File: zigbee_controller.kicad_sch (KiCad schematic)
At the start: 57 parts, among them J1 +24V, J10 IO23 load, J12 IO2 load, J13 IO, J2 5v, J4 Conn_01x07, J5 Conn_01x05, J9 IO0 load, P1 USB_C_Plug_USB2.0, Q1 IRLZ44n, Q2 IRLZ44n, Q3 IRLZ44n, SW2 EN, SW4 Joint download Boot mode, U1 TPS54560, U2 ESP32-C6-MINI-1, U3 AMS1117-3.3

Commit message: Crashed
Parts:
- removed C11, C12, C8: 22μF, Capacitor_SMD:C_1206_3216Metric_Pad1.33x1.80mm_HandSolder, symbol Device:C
- removed J13: IO, Connector_JST:JST_XH_B4B-XH-A_1x04_P2.50mm_Vertical, symbol Connector_Generic:Conn_01x04
- added C16, C17: 2.2uF, Capacitor_SMD:C_1206_3216Metric_Pad1.33x1.80mm_HandSolder, symbol Device:C
- added J3: Conn_01x06, Connector_JST:JST_XH_B6B-XH-A_1x06_P2.50mm_Vertical, symbol Connector_Generic:Conn_01x06
- added Q4, Q5, Q6: MMBT3904, Package_TO_SOT_SMD:SOT-23, symbol Transistor_BJT:MMBT3904
- added Q7: MMBT3906, Package_TO_SOT_SMD:SOT-23, symbol Transistor_BJT:MMBT3906
- added R16: 3K, symbol Device:R
- added R17: 33K, symbol Device:R
- C1, C2: value 4.7uF -> 2.2uF
- C10, C4, C9: value 22μF -> 4.7μF
- C3: value (none) -> 2.2uF; now fitted; now in the parts list
- J1, J10, J12: footprint Connector_JST:JST_VH_B2PS-VH_1x02_P3.96mm_Horizontal -> TerminalBlock:MKDS 1,5 2-5,08 P2
- J9: value IO0 load -> IO1 load; footprint Connector_JST:JST_VH_B2PS-VH_1x02_P3.96mm_Horizontal -> TerminalBlock:MKDS 1,5 2-5,08 P2
- L1: value 2.2μH -> 22μH; footprint Inductor_SMD:L_Changjiang_FXL0650 -> Inductor_SMD:L_Bourns-SRN8040_8x8.15mm
- P1: footprint Connector_USB:USB_C_Plug_ShenzhenJingTuoJin_918-118A2021Y40002_Vertical -> Connector_USB:USB_C_Receptacle_GCT_USB4105-xx-A_16P_TopMnt_Horizontal
- Q1, Q2, Q3: value IRLZ44n -> IRLB8721; footprint Package_TO_SOT_SMD:TO-263-3_TabPin2 -> Package_TO_SOT_THT:TO-220-3_Vertical
- R2: value 100k -> 51k
- R3: value 68K -> 200k
- R7: value 470k -> 220k
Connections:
- net +24V: now also C16.1, C17.1; no longer J9.1 (Pin_1)
- net +5V: now also Q4.3 (C)
- net 3V3: now also J3.1 (Pin_1)
- net GND: now also J4.7 (Pin_7), C16.2, C17.2, J3.6 (Pin_6), Q7.3 (C), R17.2; no longer J4.1 (Pin_1)
- net IO0: now also J3.4 (Pin_4); no longer J5.4 (Pin_4)
- net IO1: now also J3.5 (Pin_5), R16.1, R17.1; no longer J5.3 (Pin_3), R9.2
- net IO12-usb: now also J4.4 (Pin_4); no longer J5.2 (Pin_2)
- net IO13-usb: now also J4.3 (Pin_3); no longer J5.1 (Pin_1)
- net IO2: now also J3.2 (Pin_2)
- net IO20: now also J5.1 (Pin_1); no longer J4.7 (Pin_7)
- net IO21: now also J5.2 (Pin_2); no longer J4.6 (Pin_6)
- net IO22: now also J4.6 (Pin_6); no longer J4.5 (Pin_5)
- net IO23: now also J4.5 (Pin_5); no longer J4.4 (Pin_4)
- net IO3: now also J3.3 (Pin_3)
- net RX: now also J4.2 (Pin_2); no longer J4.3 (Pin_3)
- net TX: now also J4.1 (Pin_1); no longer J4.2 (Pin_2)
- new net: Q4.2 (E), Q7.2 (E), R9.2
- new net: Q4.1 (B), Q7.1 (B), R16.2
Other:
- moved on the sheet: J1, J9, Q1, R5, R9

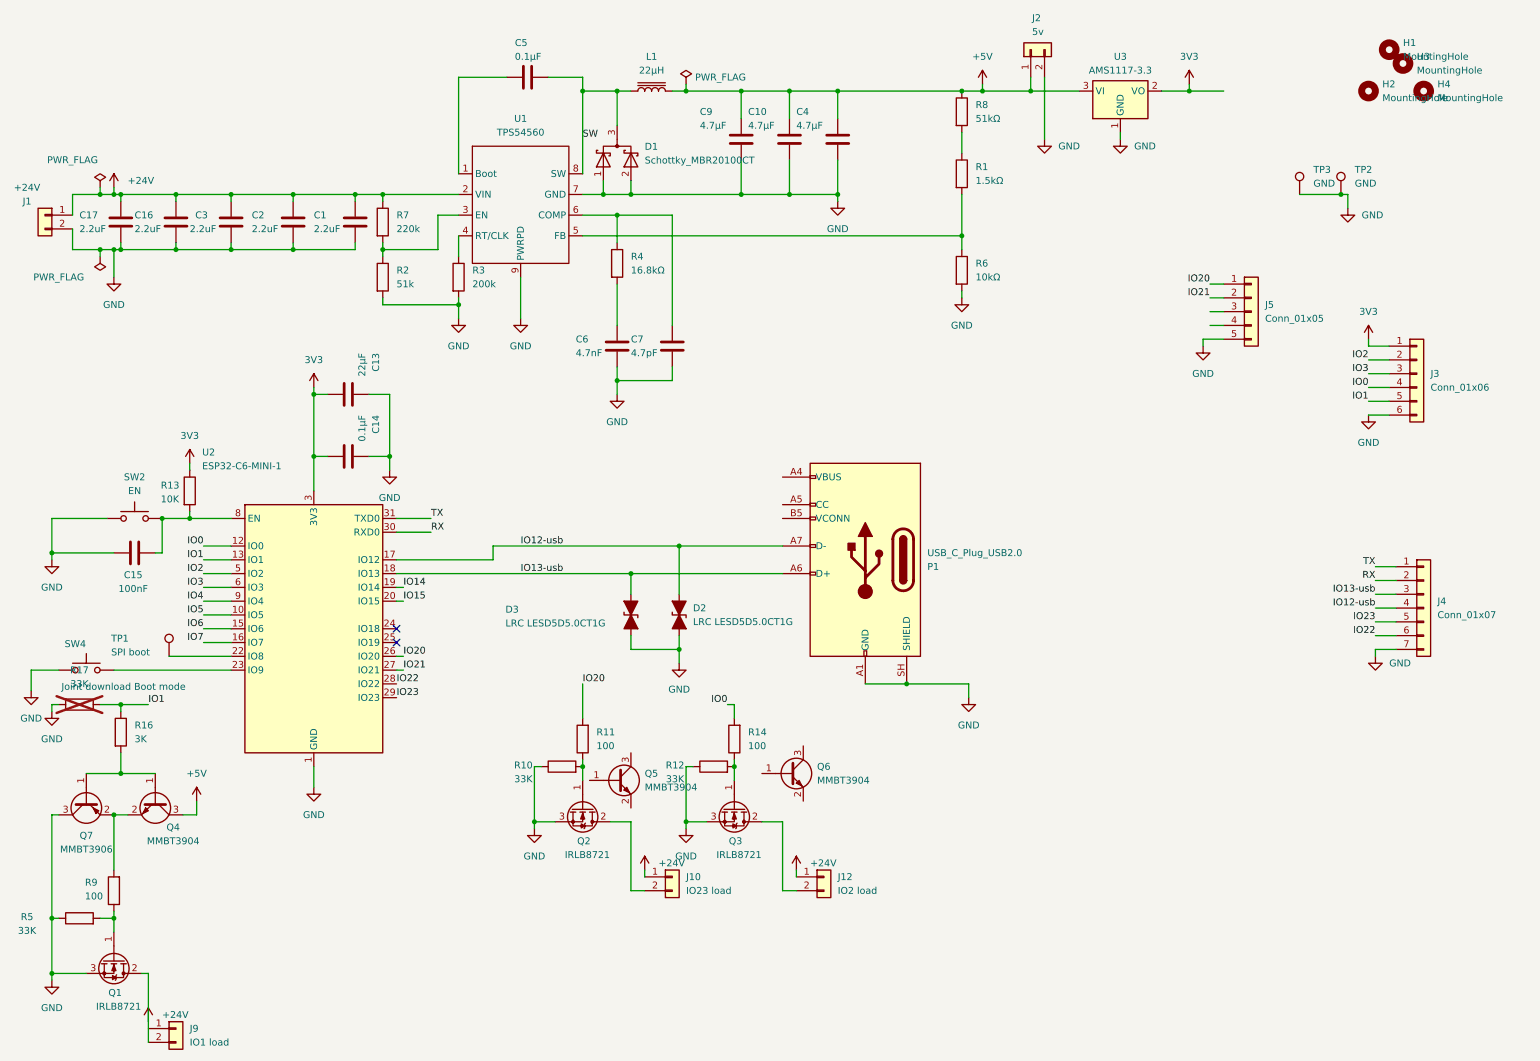
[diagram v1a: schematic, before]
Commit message: All working,  but copper pure current bottleneck
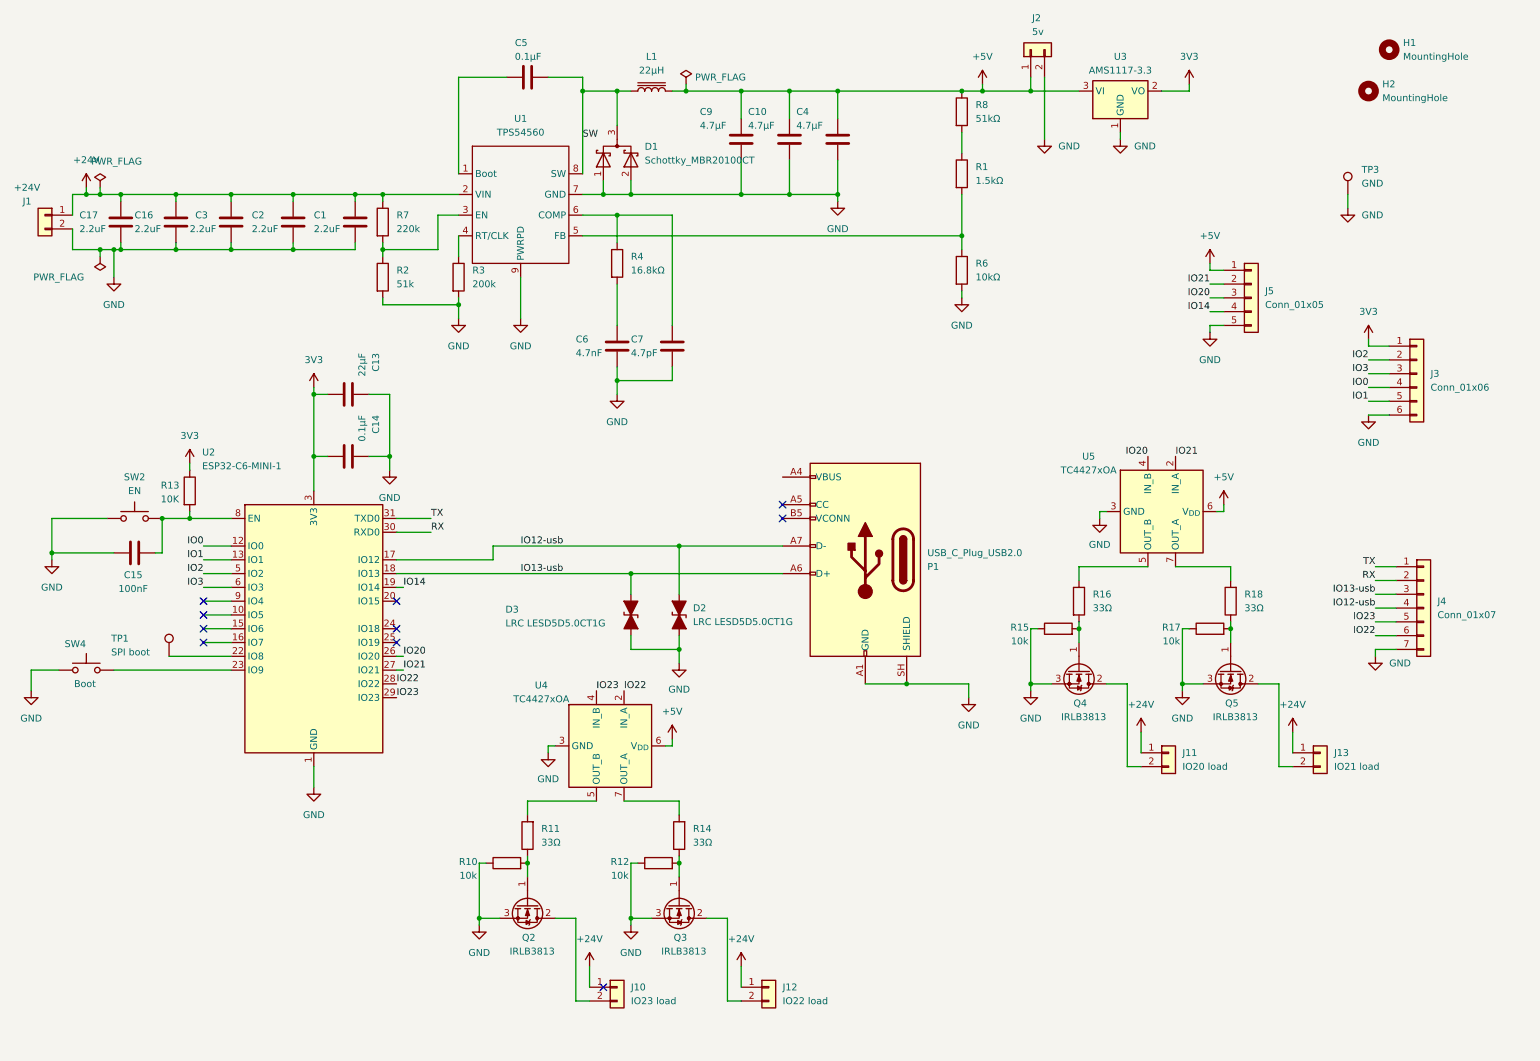
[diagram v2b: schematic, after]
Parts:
- removed H3, H4: MountingHole, MountingHole:MountingHole_2mm, symbol Mechanical:MountingHole
- removed J9: IO1 load, TerminalBlock:MKDS 1,5 2-5,08 P2, symbol Connector_Generic:Conn_01x02
- removed Q1: IRLB8721, Package_TO_SOT_THT:TO-220-3_Vertical, symbol davouds_symbol_library:IRLZ44NS
- removed Q4, Q5, Q6: MMBT3904, Package_TO_SOT_SMD:SOT-23, symbol Transistor_BJT:MMBT3904
- removed Q7: MMBT3906, Package_TO_SOT_SMD:SOT-23, symbol Transistor_BJT:MMBT3906
- removed R5: 33K, Resistor_SMD:R_1206_3216Metric_Pad1.30x1.75mm_HandSolder, symbol Device:R
- removed R9: 100, Resistor_SMD:R_1206_3216Metric_Pad1.30x1.75mm_HandSolder, symbol Device:R
- removed TP2: GND, TestPoint:TestPoint_THTPad_D2.0mm_Drill1.0mm, symbol Connector:TestPoint
- added J11: IO20 load, TerminalBlock:MKDS 1,5 2-5,08 P2, symbol Connector_Generic:Conn_01x02
- added J13: IO21 load, TerminalBlock:MKDS 1,5 2-5,08 P2, symbol Connector_Generic:Conn_01x02
- added Q4, Q5: IRLB3813, Package_TO_SOT_THT:TO-220-3_Vertical, symbol Transistor_FET:IRLB8721PBF
- added R15: 10k, Resistor_SMD:R_1206_3216Metric_Pad1.30x1.75mm_HandSolder, symbol Device:R
- added R18: 33Ω, Resistor_SMD:R_1206_3216Metric_Pad1.30x1.75mm_HandSolder, symbol Device:R
- added U4, U5: TC4427xOA, Package_SO:SOIC-8_3.9x4.9mm_P1.27mm, symbol Driver_FET:TC4427xOA
- J12: value IO2 load -> IO22 load
- Q2, Q3: value IRLB8721 -> IRLB3813; symbol davouds_symbol_library:IRLZ44NS -> Transistor_FET:IRLB8721PBF
- R10, R12: value 33K -> 10k
- R11, R14: value 100 -> 33Ω
- R16: value 3K -> 33Ω; footprint (none) -> Resistor_SMD:R_1206_3216Metric_Pad1.30x1.75mm_HandSolder
- R17: value 33K -> 10k; footprint (none) -> Resistor_SMD:R_1206_3216Metric_Pad1.30x1.75mm_HandSolder; in_stock (none) -> yes; now fitted
- SW4: value Joint download Boot mode -> Boot
- U1: footprint Package_SO:HSOP-8-1EP_3.9x4.9mm_P1.27mm_EP2.41x3.1mm_ThermalVias -> Package_SO:HSOP-8-1EP_3.9x4.9mm_P1.27mm_EP2.41x3.1mm__bigger_ThermalVias
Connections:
- net +24V: now also J11.1 (Pin_1), J13.1 (Pin_1)
- net +5V: now also J5.1 (Pin_1), U4.6 (V_{DD}), U5.6 (V_{DD})
- net GND: now also R17.1, Q4.3 (S), Q5.3 (S), R15.1, U4.3 (GND), U5.3 (GND); no longer R17.2
- net IO0: no longer R14.2
- net IO1: no longer R16.1, R17.1
- net IO14: now also J5.4 (Pin_4)
- net IO20: now also J5.3 (Pin_3), U5.4 (IN_B); no longer J5.1 (Pin_1), R11.2
- net IO21: now also U5.2 (IN_A)
- net IO22: now also U4.2 (IN_A)
- net IO23: now also U4.4 (IN_B)
- net at R16.2: now also Q4.1 (G), R15.2
- net IO15: no longer names the net of U2.20 (IO15)
- net IO4: no longer names the net of U2.9 (IO4)
- net IO5: no longer names the net of U2.10 (IO5)
- net IO6: no longer names the net of U2.15 (IO6)
- net IO7: no longer names the net of U2.16 (IO7)
- new net: Q5.1 (G), R17.2, R18.1
- new net: J13.2 (Pin_2), Q5.2 (D)
- new net: R16.1, U5.5 (OUT_B)
- new net: R14.2, U4.7 (OUT_A)
- new net: J11.2 (Pin_2), Q4.2 (D)
- new net: R18.2, U5.7 (OUT_A)
- new net: R11.2, U4.5 (OUT_B)
- no-connect marks 2 -> 10
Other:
- moved on the sheet: J10, J12, Q2, Q3, R10, R11, R12, R14, TP3

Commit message: better zoning, but need to solve one bottleneck
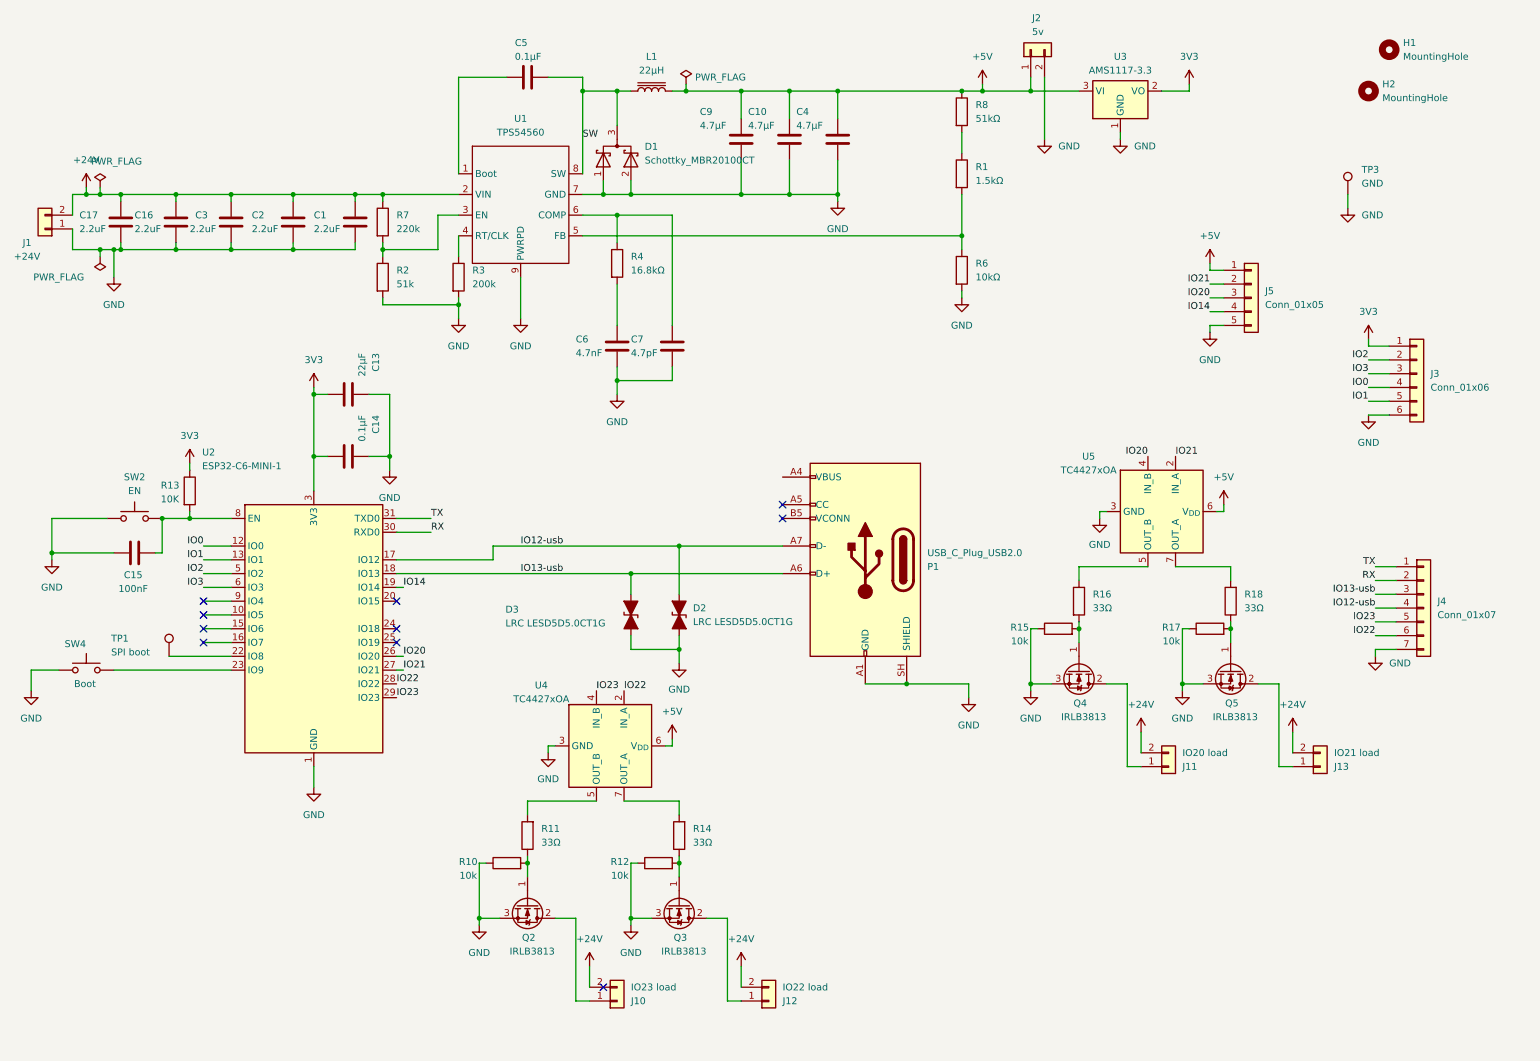
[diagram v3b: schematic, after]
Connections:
- net +24V: now also J1.2 (Pin_2), J10.2 (Pin_2), J11.2 (Pin_2), J12.2 (Pin_2), J13.2 (Pin_2); no longer J1.1 (Pin_1), J10.1 (Pin_1), J11.1 (Pin_1), J12.1 (Pin_1), J13.1 (Pin_1)
- net GND: now also J1.1 (Pin_1); no longer J1.2 (Pin_2)
- net at Q5.2 (D): now also J13.1 (Pin_1); no longer J13.2 (Pin_2)
- net at Q3.2 (D): now also J12.1 (Pin_1); no longer J12.2 (Pin_2)
- net at Q2.2 (D): now also J10.1 (Pin_1); no longer J10.2 (Pin_2)
- net at Q4.2 (D): now also J11.1 (Pin_1); no longer J11.2 (Pin_2)
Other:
- moved on the sheet: J1
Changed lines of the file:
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@@
 	(wire
 		(pts
+			(xy 21.59 50.8) (xy 21.59 46.99)
+		)
+		(stroke
+			(width 0)
+			(type default)
+		)
+	)
+	(wire
+		(pts
 			(xy 260.35 82.55) (xy 264.16 82.55)
 		)
@@
 	(wire
 		(pts
-			(xy 21.59 50.8) (xy 21.59 46.99)
-		)
-		(stroke
-			(width 0)
-			(type default)
-		)
-	)
-	(wire
-		(pts
 			(xy 82.55 119.38) (xy 81.28 119.38)
 		)
@@
 	(symbol
 		(lib_id "Connector_Generic:Conn_01x02")
-		(at 121.92 193.04 0)
+		(at 121.92 195.58 0)
+		(mirror x)
 		(unit 1)
 		(body_style 1)
@@
 		(in_pos_files yes)
 		(dnp no)
-		(fields_autoplaced yes)
 		(property "Reference" "J10"
-			(at 124.46 193.0399 0)
+			(at 124.46 195.5801 0)
 			(show_name no)
 			(do_not_autoplace no)
@@
 		)
 		(property "Value" "IO23 load"
-			(at 124.46 195.5799 0)
+			(at 124.46 193.0401 0)
 			(show_name no)
 			(do_not_autoplace no)
@@
 		)
 		(property "Footprint" "TerminalBlock:MKDS 1,5 2-5,08 P2"
-			(at 121.92 193.04 0)
+			(at 121.92 195.58 0)
 			(hide yes)
 			(show_name no)
@@
 		)
 		(property "Datasheet" ""
-			(at 121.92 193.04 0)
+			(at 121.92 195.58 0)
 			(hide yes)
 			(show_name no)
@@
 		)
 		(property "Description" "Generic connector, single row, 01x02, script generated (kicad-library-utils/schlib/autogen/connector/)"
-			(at 121.92 193.04 0)
+			(at 121.92 195.58 0)
 			(hide yes)
 			(show_name no)
@@
 	(symbol
 		(lib_id "Connector_Generic:Conn_01x02")
-		(at 16.51 50.8 0)
-		(mirror y)
+		(at 16.51 53.34 180)
 		(unit 1)
 		(body_style 1)
@@
 		(dnp no)
 		(property "Reference" "J1"
-			(at 13.208 48.26 0)
+			(at 13.208 55.88 0)
 			(show_name no)
 			(do_not_autoplace no)
@@
 		)
 		(property "Value" "+24V"
-			(at 13.208 45.72 0)
+			(at 13.208 58.42 0)
 			(show_name no)
 			(do_not_autoplace no)
@@
 		)
 		(property "Footprint" "TerminalBlock:MKDS 1,5 2-5,08 P2"
-			(at 16.51 50.8 0)
+			(at 16.51 53.34 0)
 			(hide yes)
 			(show_name no)
@@
 		)
 		(property "Datasheet" ""
-			(at 16.51 50.8 0)
+			(at 16.51 53.34 0)
 			(hide yes)
 			(show_name no)
@@
 		)
 		(property "Description" "Generic connector, single row, 01x02, script generated (kicad-library-utils/schlib/autogen/connector/)"
-			(at 16.51 50.8 0)
+			(at 16.51 53.34 0)
 			(hide yes)
 			(show_name no)
@@
 	(symbol
 		(lib_id "Connector_Generic:Conn_01x02")
-		(at 223.52 149.86 0)
+		(at 223.52 152.4 0)
+		(mirror x)
 		(unit 1)
 		(body_style 1)
@@
 		(in_pos_files yes)
 		(dnp no)
-		(fields_autoplaced yes)
 		(property "Reference" "J11"
-			(at 226.06 149.8599 0)
+			(at 226.06 152.4001 0)
 			(show_name no)
 			(do_not_autoplace no)
@@
 		)
 		(property "Value" "IO20 load"
-			(at 226.06 152.3999 0)
+			(at 226.06 149.8601 0)
 			(show_name no)
 			(do_not_autoplace no)
@@
 		)
 		(property "Footprint" "TerminalBlock:MKDS 1,5 2-5,08 P2"
-			(at 223.52 149.86 0)
+			(at 223.52 152.4 0)
 			(hide yes)
 			(show_name no)
@@
 		)
 		(property "Datasheet" ""
-			(at 223.52 149.86 0)
+			(at 223.52 152.4 0)
 			(hide yes)
 			(show_name no)
@@
 		)
 		(property "Description" "Generic connector, single row, 01x02, script generated (kicad-library-utils/schlib/autogen/connector/)"
-			(at 223.52 149.86 0)
+			(at 223.52 152.4 0)
 			(hide yes)
 			(show_name no)
@@
 	(symbol
 		(lib_id "Connector_Generic:Conn_01x02")
-		(at 149.86 193.04 0)
+		(at 149.86 195.58 0)
+		(mirror x)
 		(unit 1)
 		(body_style 1)
@@
 		(in_pos_files yes)
 		(dnp no)
-		(fields_autoplaced yes)
 		(property "Reference" "J12"
-			(at 152.4 193.0399 0)
+			(at 152.4 195.5801 0)
 			(show_name no)
 			(do_not_autoplace no)
@@
 		)
 		(property "Value" "IO22 load"
-			(at 152.4 195.5799 0)
+			(at 152.4 193.0401 0)
 			(show_name no)
 			(do_not_autoplace no)
@@
 		)
 		(property "Footprint" "TerminalBlock:MKDS 1,5 2-5,08 P2"
-			(at 149.86 193.04 0)
+			(at 149.86 195.58 0)
 			(hide yes)
 			(show_name no)
@@
 		)
 		(property "Datasheet" ""
-			(at 149.86 193.04 0)
+			(at 149.86 195.58 0)
 			(hide yes)
 			(show_name no)
@@
 		)
 		(property "Description" "Generic connector, single row, 01x02, script generated (kicad-library-utils/schlib/autogen/connector/)"
-			(at 149.86 193.04 0)
+			(at 149.86 195.58 0)
 			(hide yes)
 			(show_name no)
@@
 	(symbol
 		(lib_id "Connector_Generic:Conn_01x02")
-		(at 251.46 149.86 0)
+		(at 251.46 152.4 0)
+		(mirror x)
 		(unit 1)
 		(body_style 1)
@@
 		(in_pos_files yes)
 		(dnp no)
-		(fields_autoplaced yes)
 		(property "Reference" "J13"
-			(at 254 149.8599 0)
+			(at 254 152.4001 0)
 			(show_name no)
 			(do_not_autoplace no)
@@
 		)
 		(property "Value" "IO21 load"
-			(at 254 152.3999 0)
+			(at 254 149.8601 0)
 			(show_name no)
 			(do_not_autoplace no)
@@
 		)
 		(property "Footprint" "TerminalBlock:MKDS 1,5 2-5,08 P2"
-			(at 251.46 149.86 0)
+			(at 251.46 152.4 0)
 			(hide yes)
 			(show_name no)
@@
 		)
 		(property "Datasheet" ""
-			(at 251.46 149.86 0)
+			(at 251.46 152.4 0)
 			(hide yes)
 			(show_name no)
@@
 		)
 		(property "Description" "Generic connector, single row, 01x02, script generated (kicad-library-utils/schlib/autogen/connector/)"
-			(at 251.46 149.86 0)
+			(at 251.46 152.4 0)
 			(hide yes)
 			(show_name no)
